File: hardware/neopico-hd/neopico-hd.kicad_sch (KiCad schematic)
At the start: 1 part

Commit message: Update sch
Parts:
- removed A1: RaspberryPi_Pico, Module:RaspberryPi_Pico_Common_Unspecified, symbol MCU_Module:RaspberryPi_Pico
- added A3: WeAct_RP2350B, symbol Dudu:WeAct_RP2350B
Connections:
- net B0: now also A3.43 (GPIO37)
- net B1: now also A3.42 (GPIO36)
- net B2: now also A3.41 (GPIO35)
- net B3: now also A3.40 (GPIO34)
- net B4: now also A3.39 (GPIO33)
- net G0: now also A3.48 (GPIO42)
- net G1: now also A3.47 (GPIO41)
- net G2: now also A3.46 (GPIO40)
- net G3: now also A3.45 (GPIO39)
- net G4: now also A3.44 (GPIO38)
- net R0: now also A3.54 (GPIO47)
- net R1: now also A3.53 (GPIO46)
- net R2: now also A3.52 (GPIO45)
- net R3: now also A3.51 (GPIO44)
- net R4: now also A3.50 (GPIO43)
- new net CSYNC: A3.36 (GPIO30)
- new net DARK: A3.38 (GPIO32)
- new net PCKL: A3.35 (GPIO29)
- new net SHADOW: A3.37 (GPIO31)
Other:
- company: (none) -> https://www.github.com/fliperama86/neopico-hd
- title: (none) -> NeoPico HD

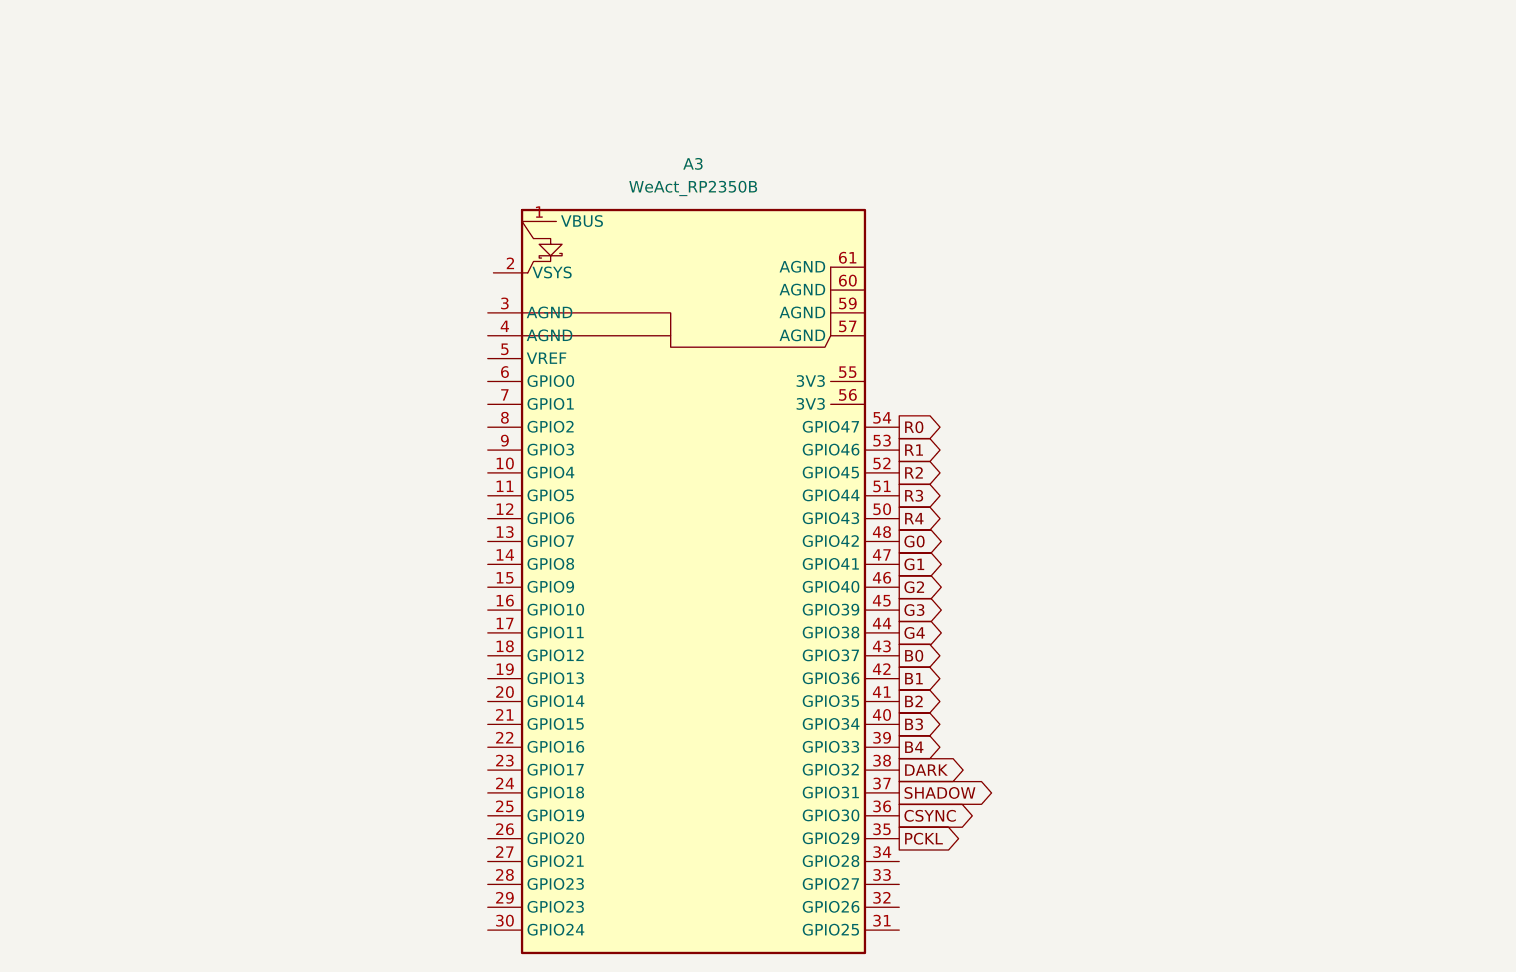
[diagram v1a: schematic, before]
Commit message: Update prototype sch
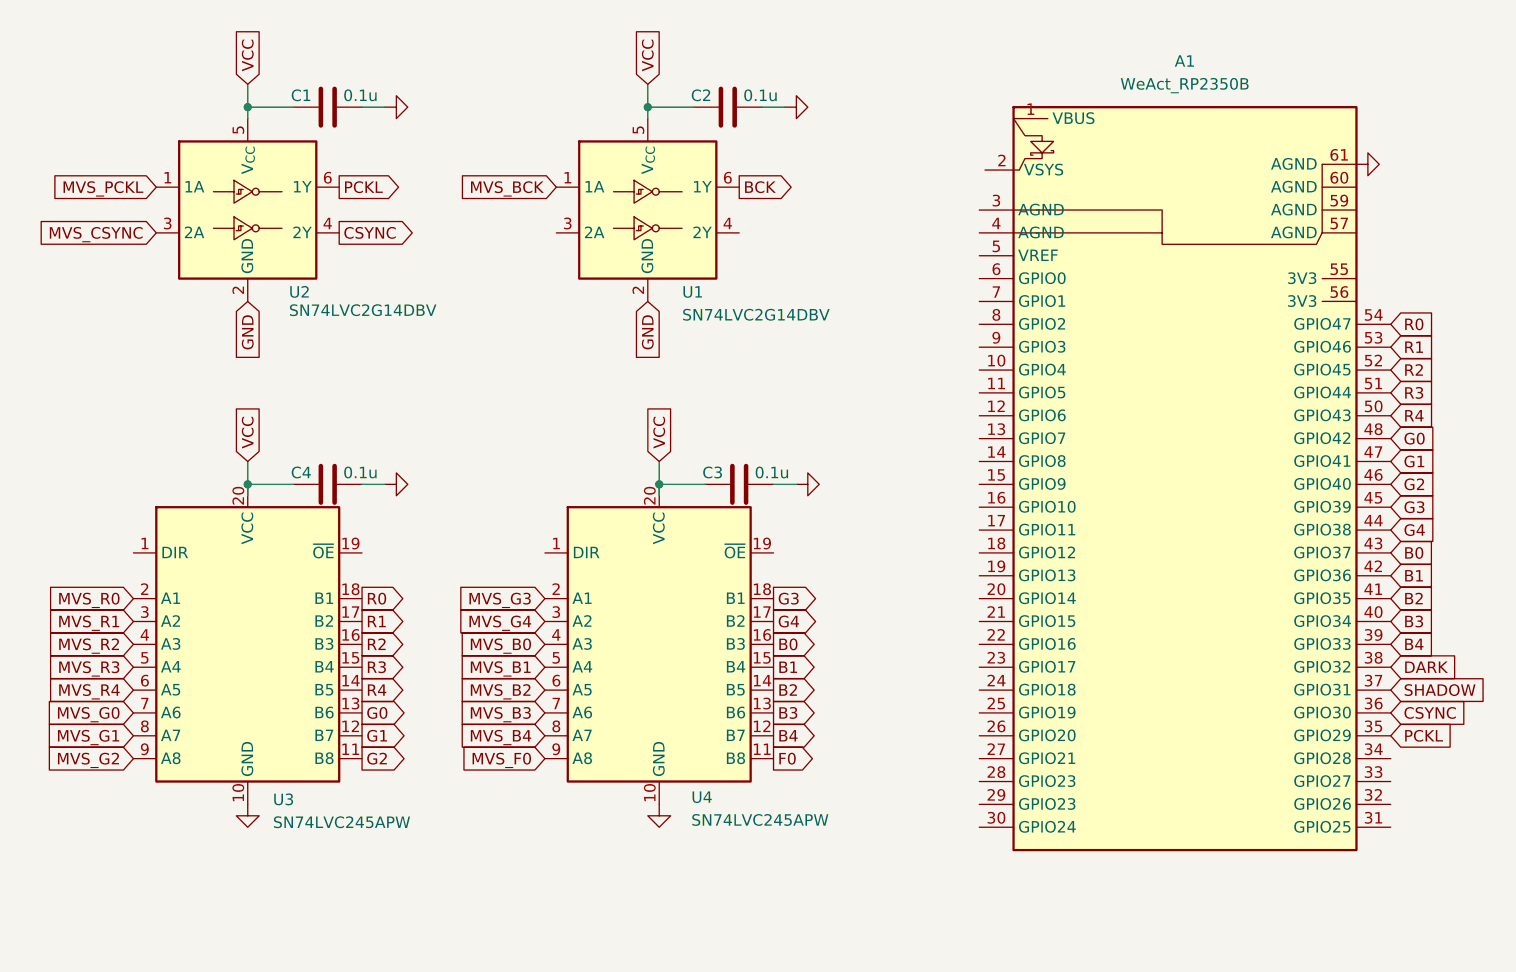
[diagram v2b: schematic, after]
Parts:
- added C1, C2, C3, C4: 0.1u, custom_components:SM0603_Capa_libcms, symbol Device:C
- added U1, U2: SN74LVC2G14DBV, Package_TO_SOT_SMD:SOT-23-6, symbol 74xGxx:SN74LVC2G14DBV
- added U3, U4: SN74LVC245APW, Package_SO:TSSOP-20_4.4x6.5mm_P0.65mm, symbol Logic_LevelTranslator:SN74LVC245APW
- renumbered A3 to A1
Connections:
- net B0: now also U4.16 (B3)
- net B1: now also U4.15 (B4)
- net B2: now also U4.14 (B5)
- net B3: now also U4.13 (B6)
- net B4: now also U4.12 (B7)
- net CSYNC: now also U2.4 (2Y)
- net G0: now also U3.13 (B6)
- net G1: now also U3.12 (B7)
- net G2: now also U3.11 (B8)
- net G3: now also U4.18 (B1)
- net G4: now also U4.17 (B2)
- net PCKL: now also U2.6 (1Y)
- net R0: now also U3.18 (B1)
- net R1: now also U3.17 (B2)
- net R2: now also U3.16 (B3)
- net R3: now also U3.15 (B4)
- net R4: now also U3.14 (B5)
- net GND: now reaches A1.61 (AGND)
- net GND: now also C1.2, C2.2, C3.2, C4.2, U1.2 (GND), U2.2 (GND), U3.10 (GND), U4.10 (GND)
- new net BCK: U1.6 (1Y)
- new net F0: U4.11 (B8)
- new net MVS_B0: U4.4 (A3)
- new net MVS_B1: U4.5 (A4)
- new net MVS_B2: U4.6 (A5)
- new net MVS_B3: U4.7 (A6)
- new net MVS_B4: U4.8 (A7)
- new net MVS_BCK: U1.1 (1A)
- new net MVS_CSYNC: U2.3 (2A)
- new net MVS_F0: U4.9 (A8)
- new net MVS_G0: U3.7 (A6)
- new net MVS_G1: U3.8 (A7)
- new net MVS_G2: U3.9 (A8)
- new net MVS_G3: U4.2 (A1)
- new net MVS_G4: U4.3 (A2)
- new net MVS_PCKL: U2.1 (1A)
- new net MVS_R0: U3.2 (A1)
- new net MVS_R1: U3.3 (A2)
- new net MVS_R2: U3.4 (A3)
- new net MVS_R3: U3.5 (A4)
- new net MVS_R4: U3.6 (A5)
- new net VCC: C1.1, C2.1, C3.1, C4.1, U1.5 (V_{CC}), U2.5 (V_{CC}), U3.20 (VCC), U4.20 (VCC)
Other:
- moved on the sheet: A1
